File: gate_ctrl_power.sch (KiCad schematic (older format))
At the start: 14 parts

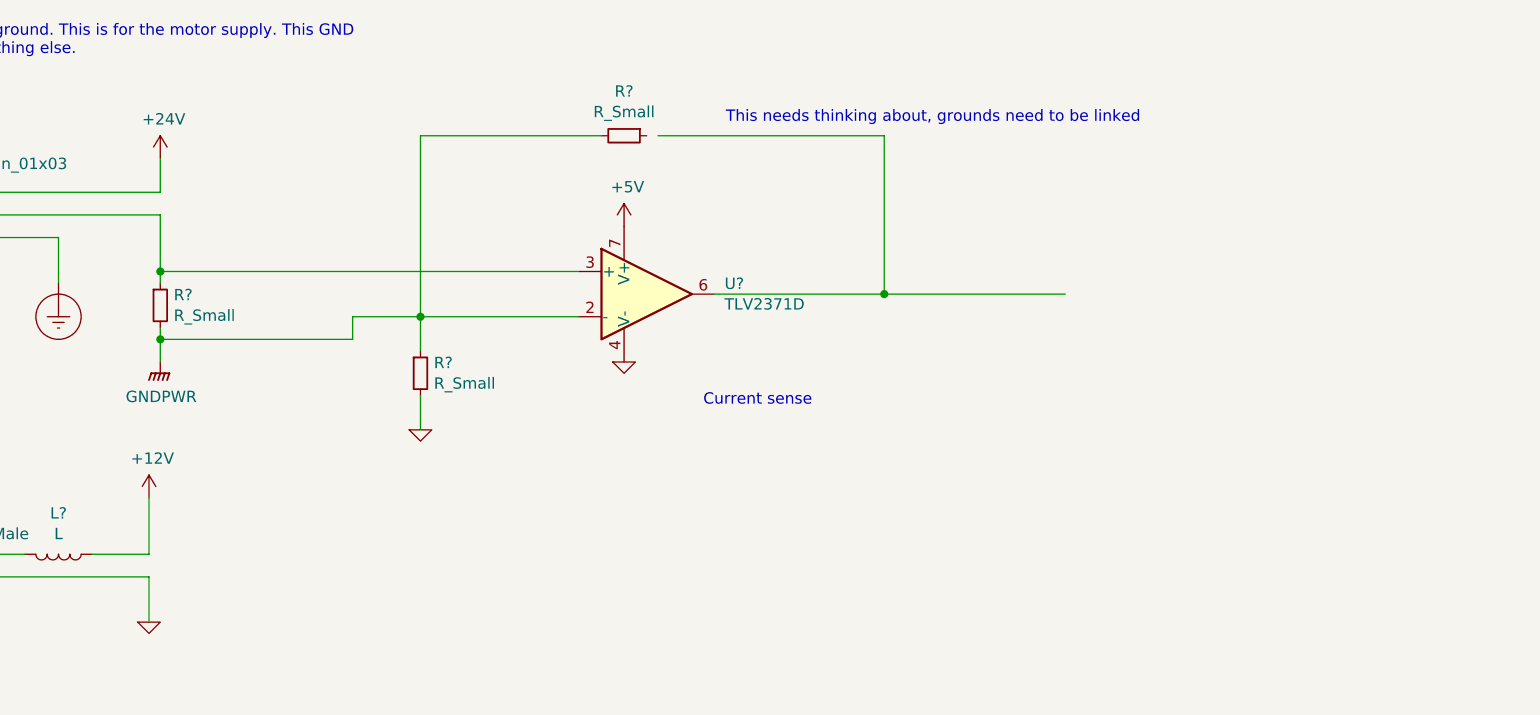
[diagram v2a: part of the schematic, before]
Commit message: Added current sense filter
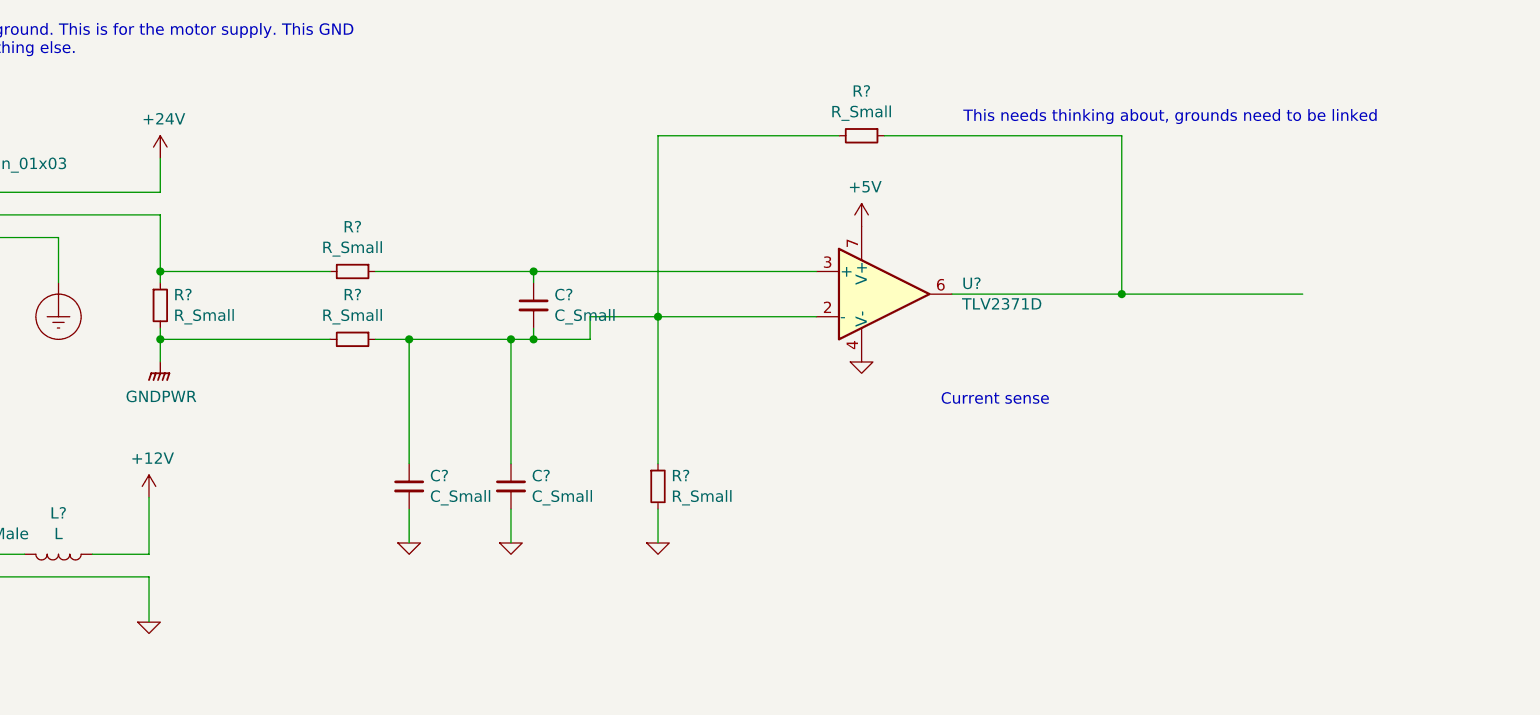
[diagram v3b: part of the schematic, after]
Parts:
- added C? (x3): C_Small, symbol Device:C_Small
- added R? (x2): R_Small, symbol Device:R_Small
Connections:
- wire segments 53 -> 65
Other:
- moved on the sheet: R?, U?
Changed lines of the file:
@@
 L Amplifier_Operational:TLV2371D U?
 U 1 1 5F6CA701
-P 4750 1900
-F 0 "U?" H 5094 1946 50  0000 L CNN
-F 1 "TLV2371D" H 5094 1855 50  0000 L CNN
-F 2 "Package_SO:SOIC-8_3.9x4.9mm_P1.27mm" H 4650 1700 50  0001 L CNN
-F 3 "http://www.ti.com/lit/ds/symlink/tlv2375.pdf" H 4900 2050 50  0001 C CNN
-	1    4750 1900
+P 5800 1900
+F 0 "U?" H 6144 1946 50  0000 L CNN
+F 1 "TLV2371D" H 6144 1855 50  0000 L CNN
+F 2 "Package_SO:SOIC-8_3.9x4.9mm_P1.27mm" H 5700 1700 50  0001 L CNN
+F 3 "http://www.ti.com/lit/ds/symlink/tlv2375.pdf" H 5950 2050 50  0001 C CNN
+	1    5800 1900
 	1    0    0    -1
 $EndComp
@@
 $EndComp
 Wire Wire Line
-	2600 1550 2600 1800
-Wire Wire Line
-	2600 2050 2600 2100
-Wire Wire Line
-	4450 1800 2600 1800
-Connection ~ 2600 1800
-Wire Wire Line
-	2600 1800 2600 1850
-Wire Wire Line
-	4450 2000 3750 2000
-Wire Wire Line
-	3450 2000 3450 2100
-Wire Wire Line
-	3450 2100 2600 2100
-Connection ~ 2600 2100
-Wire Wire Line
-	2600 2100 2600 2200
-Text Notes 5100 1150 0    50   ~ 0
+	5500 1800 4250 1800
+Wire Wire Line
+	5500 2000 4800 2000
+Wire Wire Line
+	4500 2000 4500 2100
+Wire Wire Line
+	4500 2100 4250 2100
+Text Notes 6150 1150 0    50   ~ 0
 This needs thinking about, grounds need to be linked
 $Comp
 L power:+5V #PWR?
 U 1 1 5F6CFCC9
-P 4650 1600
-F 0 "#PWR?" H 4650 1450 50  0001 C CNN
-F 1 "+5V" H 4665 1773 50  0000 C CNN
-F 2 "" H 4650 1600 50  0001 C CNN
-F 3 "" H 4650 1600 50  0001 C CNN
-	1    4650 1600
+P 5700 1600
+F 0 "#PWR?" H 5700 1450 50  0001 C CNN
+F 1 "+5V" H 5715 1773 50  0000 C CNN
+F 2 "" H 5700 1600 50  0001 C CNN
+F 3 "" H 5700 1600 50  0001 C CNN
+	1    5700 1600
 	1    0    0    -1
 $EndComp
@@
 L Microtan_65_CPU-cache:GND #PWR?
 U 1 1 5F6D0394
-P 4650 2200
-F 0 "#PWR?" H 4650 2200 30  0001 C CNN
-F 1 "GND" H 4650 2130 30  0001 C CNN
-F 2 "" H 4650 2200 60  0000 C CNN
-F 3 "" H 4650 2200 60  0000 C CNN
-	1    4650 2200
+P 5700 2200
+F 0 "#PWR?" H 5700 2200 30  0001 C CNN
+F 1 "GND" H 5700 2130 30  0001 C CNN
+F 2 "" H 5700 2200 60  0000 C CNN
+F 3 "" H 5700 2200 60  0000 C CNN
+	1    5700 2200
 	1    0    0    -1
 $EndComp
@@
 L Device:R_Small R?
 U 1 1 5F6D17FE
-P 4650 1200
-F 0 "R?" V 4454 1200 50  0000 C CNN
-F 1 "R_Small" V 4545 1200 50  0000 C CNN
-F 2 "" H 4650 1200 50  0001 C CNN
-F 3 "~" H 4650 1200 50  0001 C CNN
-	1    4650 1200
+P 5700 1200
+F 0 "R?" V 5504 1200 50  0000 C CNN
+F 1 "R_Small" V 5595 1200 50  0000 C CNN
+F 2 "" H 5700 1200 50  0001 C CNN
+F 3 "~" H 5700 1200 50  0001 C CNN
+	1    5700 1200
 	0    1    1    0
 $EndComp
@@
 L Device:R_Small R?
 U 1 1 5F6D20B0
-P 3750 2250
-F 0 "R?" H 3809 2296 50  0000 L CNN
-F 1 "R_Small" H 3809 2205 50  0000 L CNN
-F 2 "" H 3750 2250 50  0001 C CNN
-F 3 "~" H 3750 2250 50  0001 C CNN
-	1    3750 2250
+P 4800 2750
+F 0 "R?" H 4859 2796 50  0000 L CNN
+F 1 "R_Small" H 4859 2705 50  0000 L CNN
+F 2 "" H 4800 2750 50  0001 C CNN
+F 3 "~" H 4800 2750 50  0001 C CNN
+	1    4800 2750
 	1    0    0    -1
 $EndComp
@@
 L Microtan_65_CPU-cache:GND #PWR?
 U 1 1 5F6D2B1C
-P 3750 2500
-F 0 "#PWR?" H 3750 2500 30  0001 C CNN
-F 1 "GND" H 3750 2430 30  0001 C CNN
-F 2 "" H 3750 2500 60  0000 C CNN
-F 3 "" H 3750 2500 60  0000 C CNN
-	1    3750 2500
-	1    0    0    -1
-$EndComp
-Wire Wire Line
-	3750 2500 3750 2350
-Wire Wire Line
-	3750 2150 3750 2000
-Connection ~ 3750 2000
-Wire Wire Line
-	3750 2000 3450 2000
-Wire Wire Line
-	3750 2000 3750 1200
-Wire Wire Line
-	3750 1200 4550 1200
-Wire Wire Line
-	4800 1200 5800 1200
-Wire Wire Line
-	5800 1200 5800 1900
-Wire Wire Line
-	5800 1900 5050 1900
-Wire Wire Line
-	5800 1900 6600 1900
-Connection ~ 5800 1900
-Text Notes 5000 2400 0    50   ~ 0
+P 4800 3000
+F 0 "#PWR?" H 4800 3000 30  0001 C CNN
+F 1 "GND" H 4800 2930 30  0001 C CNN
+F 2 "" H 4800 3000 60  0000 C CNN
+F 3 "" H 4800 3000 60  0000 C CNN
+	1    4800 3000
+	1    0    0    -1
+$EndComp
+Wire Wire Line
+	4800 3000 4800 2850
+Wire Wire Line
+	4800 2650 4800 2000
+Connection ~ 4800 2000
+Wire Wire Line
+	4800 2000 4500 2000
+Wire Wire Line
+	4800 2000 4800 1200
+Wire Wire Line
+	4800 1200 5600 1200
+Wire Wire Line
+	6850 1200 6850 1900
+Wire Wire Line
+	6850 1900 6100 1900
+Wire Wire Line
+	6850 1900 7650 1900
+Connection ~ 6850 1900
+Text Notes 6050 2400 0    50   ~ 0
 Current sense
+Wire Wire Line
+	5800 1200 6850 1200
+$Comp
+L Device:C_Small C?
+U 1 1 5F6DD4A0
+P 4250 1950
+F 0 "C?" H 4342 1996 50  0000 L CNN
+F 1 "C_Small" H 4342 1905 50  0000 L CNN
+F 2 "" H 4250 1950 50  0001 C CNN
+F 3 "~" H 4250 1950 50  0001 C CNN
+	1    4250 1950
+	1    0    0    -1
+$EndComp
+$Comp
+L Device:C_Small C?
+U 1 1 5F6DDC55
+P 3700 2750
+F 0 "C?" H 3792 2796 50  0000 L CNN
+F 1 "C_Small" H 3792 2705 50  0000 L CNN
+F 2 "" H 3700 2750 50  0001 C CNN
+F 3 "~" H 3700 2750 50  0001 C CNN
+	1    3700 2750
+	1    0    0    -1
+$EndComp
+$Comp
+L Device:C_Small C?
+U 1 1 5F6DED41
+P 4150 2750
+F 0 "C?" H 4242 2796 50  0000 L CNN
+F 1 "C_Small" H 4242 2705 50  0000 L CNN
+F 2 "" H 4150 2750 50  0001 C CNN
+F 3 "~" H 4150 2750 50  0001 C CNN
+	1    4150 2750
+	1    0    0    -1
+$EndComp
+Wire Wire Line
+	4250 1850 4250 1800
+Wire Wire Line
+	4250 2050 4250 2100
+Wire Wire Line
+	2600 1550 2600 1800
+Wire Wire Line
+	2600 2050 2600 2100
+$Comp
+L Device:R_Small R?
+U 1 1 5F6EA220
+P 3450 1800
+F 0 "R?" V 3254 1800 50  0000 C CNN
+F 1 "R_Small" V 3345 1800 50  0000 C CNN
+F 2 "" H 3450 1800 50  0001 C CNN
+F 3 "~" H 3450 1800 50  0001 C CNN
+	1    3450 1800
+	0    1    1    0
+$EndComp
+$Comp
+L Device:R_Small R?
+U 1 1 5F6EB19E
+P 3450 2100
+F 0 "R?" V 3254 2100 50  0000 C CNN
+F 1 "R_Small" V 3345 2100 50  0000 C CNN
+F 2 "" H 3450 2100 50  0001 C CNN
+F 3 "~" H 3450 2100 50  0001 C CNN
+	1    3450 2100
+	0    1    1    0
+$EndComp
+Wire Wire Line
+	3350 2100 2600 2100
+Connection ~ 2600 2100
+Wire Wire Line
+	2600 2100 2600 2200
+Wire Wire Line
+	3350 1800 2600 1800
+Connection ~ 2600 1800
+Wire Wire Line
+	2600 1800 2600 1850
+Wire Wire Line
+	3550 1800 4250 1800
+Connection ~ 4250 1800
+Wire Wire Line
+	3550 2100 3700 2100
+Connection ~ 4250 2100
+$Comp
+L Microtan_65_CPU-cache:GND #PWR?
+U 1 1 5F6F0720
+P 3700 3000
+F 0 "#PWR?" H 3700 3000 30  0001 C CNN
+F 1 "GND" H 3700 2930 30  0001 C CNN
+F 2 "" H 3700 3000 60  0000 C CNN
+F 3 "" H 3700 3000 60  0000 C CNN
+	1    3700 3000
+	1    0    0    -1
+$EndComp
+$Comp
+L Microtan_65_CPU-cache:GND #PWR?
+U 1 1 5F6F0B91
+P 4150 3000
+F 0 "#PWR?" H 4150 3000 30  0001 C CNN
+F 1 "GND" H 4150 2930 30  0001 C CNN
+F 2 "" H 4150 3000 60  0000 C CNN
+F 3 "" H 4150 3000 60  0000 C CNN
+	1    4150 3000
+	1    0    0    -1
+$EndComp
+Wire Wire Line
+	4150 2850 4150 3000
+Wire Wire Line
+	4150 2650 4150 2100
+Connection ~ 4150 2100
+Wire Wire Line
+	4150 2100 4250 2100
+Wire Wire Line
+	3700 2650 3700 2100
+Connection ~ 3700 2100
+Wire Wire Line
+	3700 2100 4150 2100
+Wire Wire Line
+	3700 2850 3700 3000
 $EndSCHEMATC
